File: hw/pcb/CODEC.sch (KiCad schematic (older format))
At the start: 55 parts, among them J501 AUEXT, J502 RIN, J503 LIN, J504 ROUT, J505 LOUT, U501 WM8731, U502 TL072, U503 TL072, Y501 11.289600

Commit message: wm8978 PCB design files
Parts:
- removed C521: 10u, Capacitor_SMD:C_0402_1005Metric, symbol Device:C
- removed J501: AUEXT, Connector_PinHeader_2.54mm:PinHeader_2x05_P2.54mm_Vertical_SMD, symbol Connector_Generic:Conn_02x05_Odd_Even
- removed U501: WM8731, Package_SO:SSOP-28_5.3x10.2mm_P0.65mm, symbol cirrus:WM8731
- removed Y501: 11.289600, Crystal:Crystal_SMD_3225-4Pin_3.2x2.5mm, symbol Device:Crystal_GND24
- added JP505: ROUT, Jumper:SolderJumper-3_P1.3mm_Open_RoundedPad1.0x1.5mm_NumberLabels, symbol Jumper:Jumper_3_Open
- added JP506: LOUT, Jumper:SolderJumper-3_P1.3mm_Open_RoundedPad1.0x1.5mm_NumberLabels, symbol Jumper:Jumper_3_Open
- added JP507: LIN, Jumper:SolderJumper-3_P1.3mm_Open_RoundedPad1.0x1.5mm_NumberLabels, symbol Jumper:Jumper_3_Open
- added JP508: RIN, Jumper:SolderJumper-3_P1.3mm_Open_RoundedPad1.0x1.5mm_NumberLabels, symbol Jumper:Jumper_3_Open
- added L501: 10uH, Capacitor_SMD:C_0603_1608Metric, symbol Device:L
- added U501: WM8978CGEFL_V, Package_DFN_QFN:QFN-32-1EP_5x5mm_P0.5mm_EP3.65x3.65mm_ThermalVias, symbol SamacSys_Parts:WM8978CGEFL_V
- C502, C514, C520: value 10u -> 100n
- C503, C508: value 100n -> 4.7u
- C505, C506: value 18p -> 4.7u
- C507: value 10u -> 4.7u
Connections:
- net labels added: +3.3VP, L2, MCLK, R2
- net labels removed: LHPOUT, MICBIAS, MICIN, RHPOUT
- wire segments 236 -> 221
- no-connect marks 5 -> 9
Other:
- note added: "Bridge solder jumpers on pin 2+3 for normal operations.\n1+2 is for testing and playing with the codec."
- note added: "Solder jumpers for DC coupling (not tested)"
- note added: "The output op amp section is based on\nMutable Instruments Clouds (c) Émilie Gillet"
- note added: "WM8978 ADC is MUCH BETTER than the WM8731:\nRead this also: https://hackaday.io/project/7936-cortex-guitar-board/log/44553-this-adc-makes-weird-noises\nIt strikes me that it is still used so often in Eurorack audio (I made that mistake too)"
- note removed: "This section is based on\nMutable Instruments Clouds (c) Émilie Gillet"
- note removed: "To external audio breakout.\nUseful for testing."
- moved on the sheet: C507, C511, C515, C516, C517, C522, C523, C524, J504, J505, JP503, JP504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

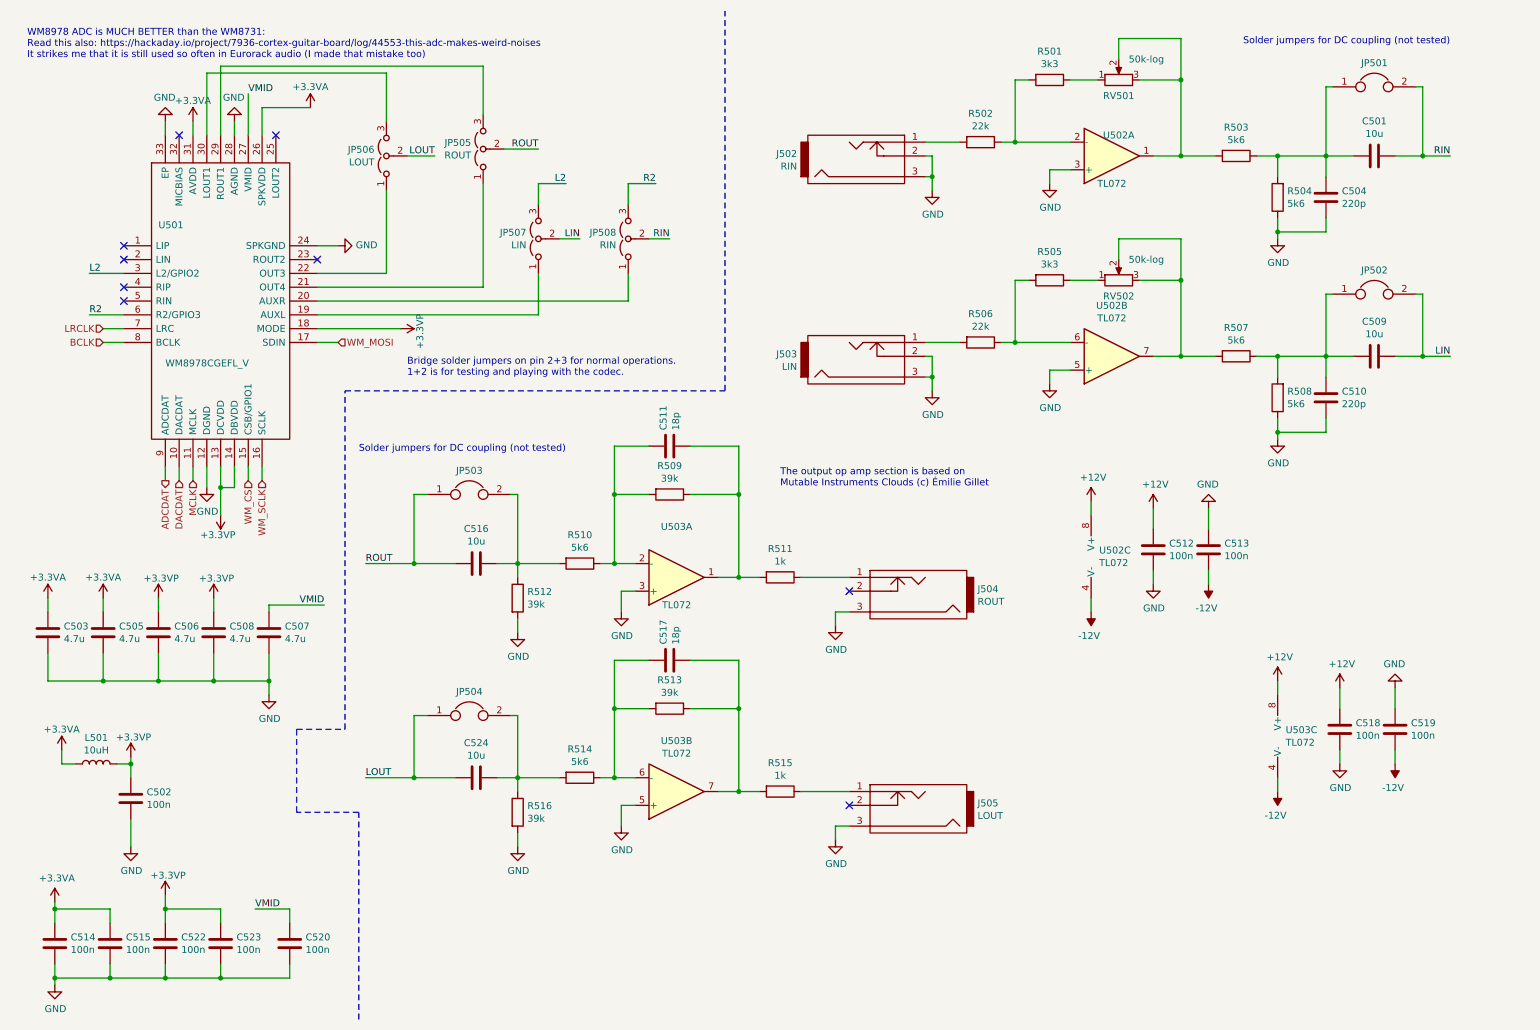
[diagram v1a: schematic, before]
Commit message: fixed severe PCB issue, clearance of ground fills was too small, could lead to thermal instability
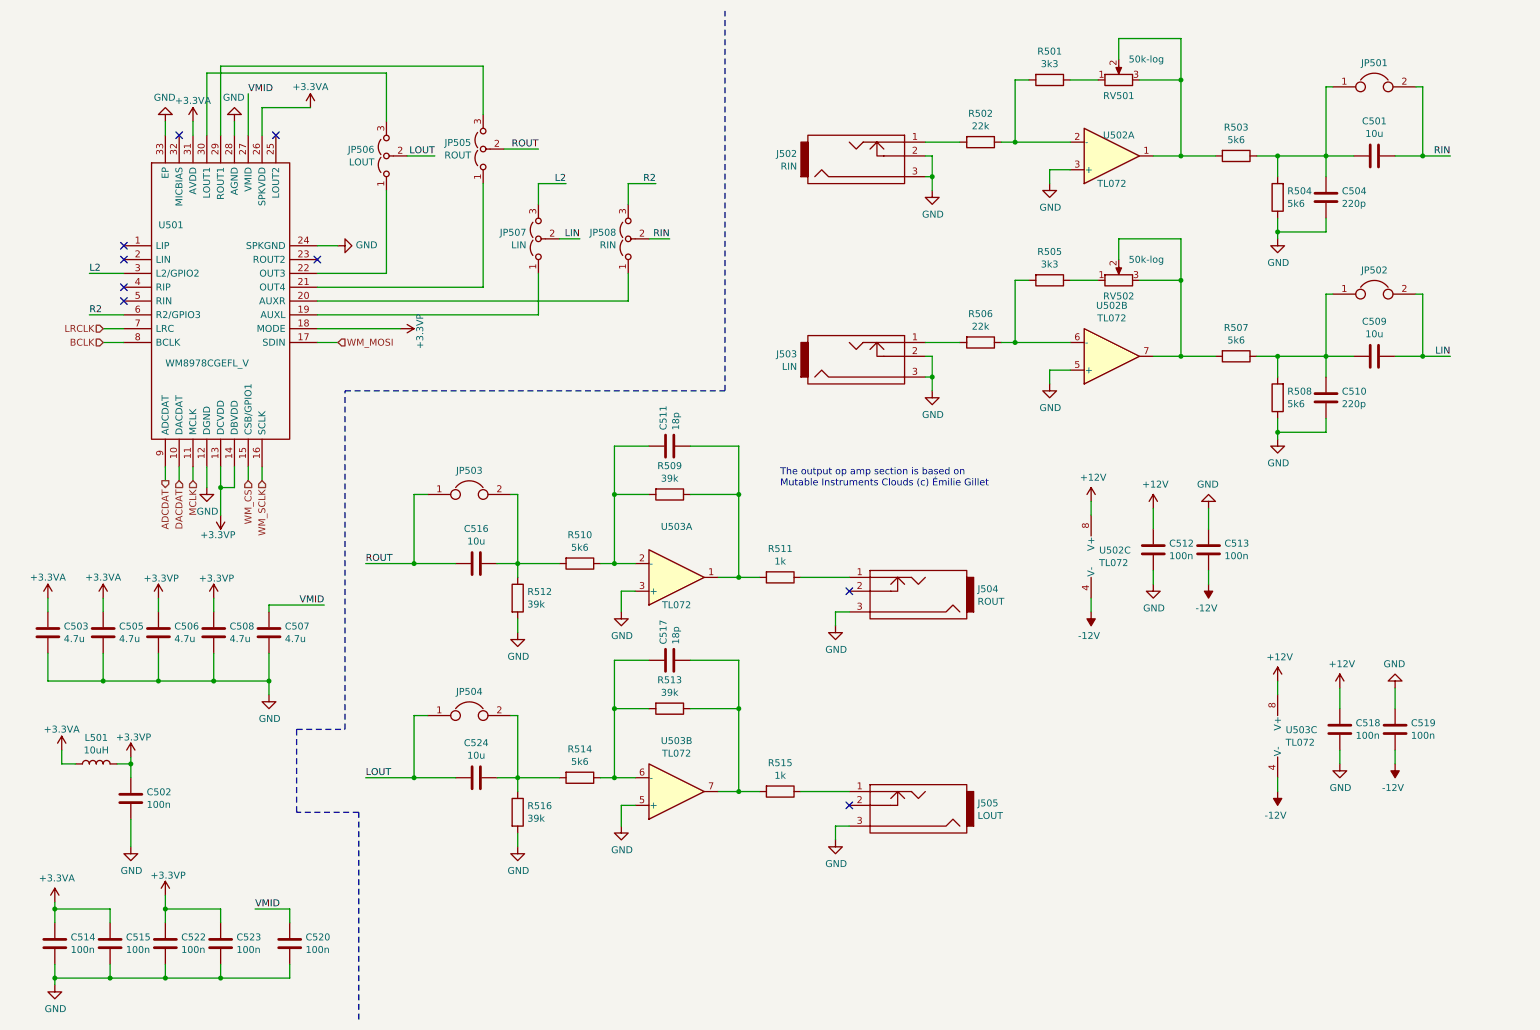
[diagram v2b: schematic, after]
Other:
- note removed: "Bridge solder jumpers on pin 2+3 for normal operations.\n1+2 is for testing and playing with the codec."
- note removed: "Solder jumpers for DC coupling (not tested)"
- note removed: "WM8978 ADC is MUCH BETTER than the WM8731:\nRead this also: https://hackaday.io/project/7936-cortex-guitar-board/log/44553-this-adc-makes-weird-noises\nIt strikes me that it is still used so often in Eurorack audio (I made that mistake too)"
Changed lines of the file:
@@
 encoding utf-8
 Sheet 5 6
-Title "CTAG-TBD"
-Date "2020-06-06"
-Rev "C"
+Title "ESP32 Eurorack Audio Module"
+Date "2020-08-18"
+Rev "G"
 Comp "(c) Robert Manzke 2020"
 Comment1 "https://creativecommons.org/licenses/by-nc-sa/4.0/"
@@
 Wire Wire Line
 	4300 2650 4300 2350
-Text Notes 600  800  0    50   ~ 0
-WM8978 ADC is MUCH BETTER than the WM8731:\nRead this also: https://hackaday.io/project/7936-cortex-guitar-board/log/44553-this-adc-makes-weird-noises\nIt strikes me that it is still used so often in Eurorack audio (I made that mistake too)
-Text Notes 3000 3650 0    50   ~ 0
-Solder jumpers for DC coupling (not tested)
-Text Notes 9400 700  0    50   ~ 0
-Solder jumpers for DC coupling (not tested)
-Text Notes 3350 3100 0    50   ~ 0
-Bridge solder jumpers on pin 2+3 for normal operations.\n1+2 is for testing and playing with the codec.
 $EndSCHEMATC

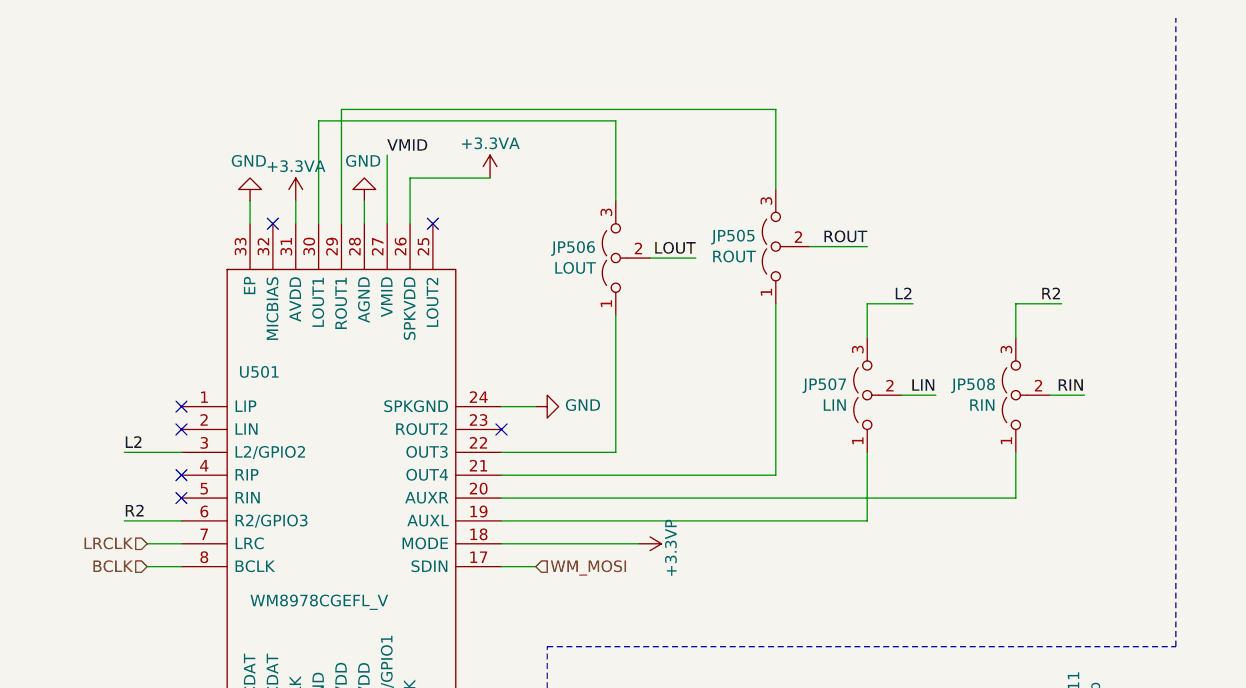
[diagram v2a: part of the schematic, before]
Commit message: Updated Eurorack hw to Rev. H
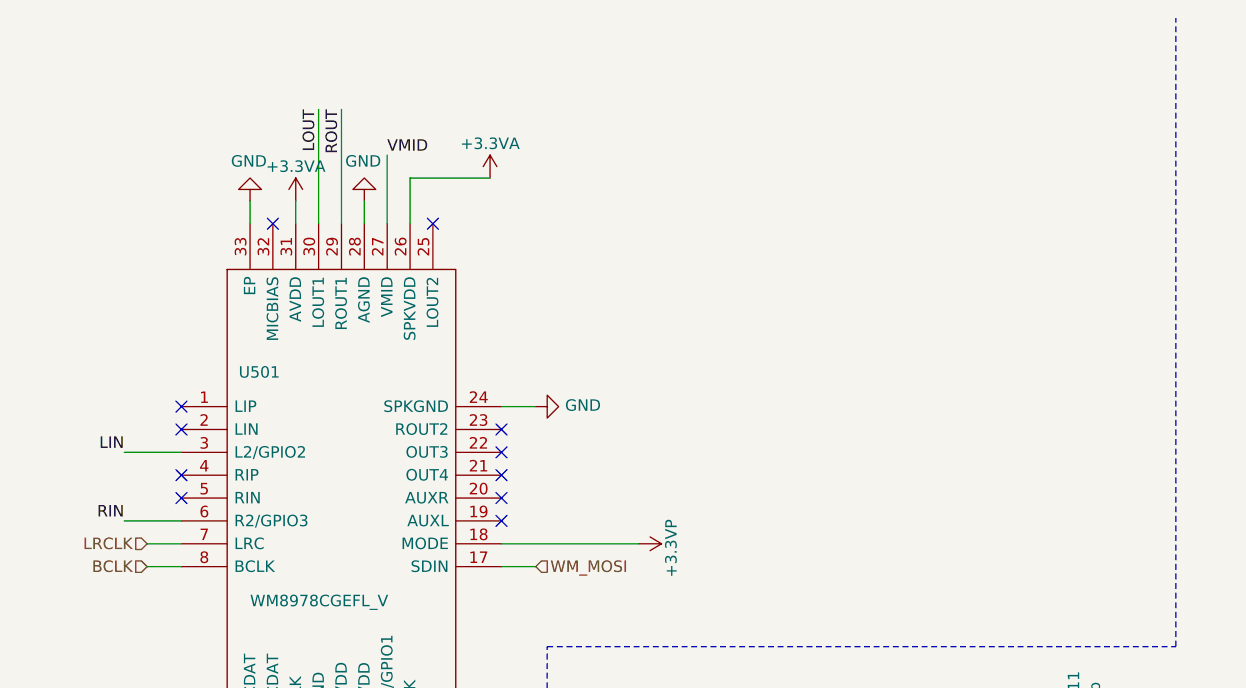
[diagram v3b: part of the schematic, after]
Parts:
- removed JP505: ROUT, Jumper:SolderJumper-3_P1.3mm_Open_RoundedPad1.0x1.5mm_NumberLabels, symbol Jumper:Jumper_3_Open
- removed JP506: LOUT, Jumper:SolderJumper-3_P1.3mm_Open_RoundedPad1.0x1.5mm_NumberLabels, symbol Jumper:Jumper_3_Open
- removed JP507: LIN, Jumper:SolderJumper-3_P1.3mm_Open_RoundedPad1.0x1.5mm_NumberLabels, symbol Jumper:Jumper_3_Open
- removed JP508: RIN, Jumper:SolderJumper-3_P1.3mm_Open_RoundedPad1.0x1.5mm_NumberLabels, symbol Jumper:Jumper_3_Open
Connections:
- net L2 is gone; now on net LIN: U501.3 (L2/GPIO2)
- net R2 is gone; now on net RIN: U501.6 (R2/GPIO3)
- net LOUT: now also U501.30 (LOUT1)
- net ROUT: now also U501.29 (ROUT1)
- no-connect marks 9 -> 13
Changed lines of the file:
@@
 Sheet 5 6
 Title "ESP32 Eurorack Audio Module"
-Date "2020-08-18"
-Rev "G"
-Comp "(c) Robert Manzke 2020"
+Date "2021-10-05"
+Rev "H"
+Comp "(c) Robert Manzke 2021"
 Comment1 "https://creativecommons.org/licenses/by-nc-sa/4.0/"
 Comment2 "Licensed under CC BY-NC-SA 4.0"
@@
 Wire Wire Line
 	2350 4750 2750 4750
-Wire Wire Line
-	4050 1450 4300 1450
-Text Label 3550 1500 2    50   ~ 0
+Text Label 1900 850  3    50   ~ 0
 LOUT
-Text Label 4300 1450 2    50   ~ 0
+Text Label 2000 850  3    50   ~ 0
 ROUT
 Text Label 2750 4750 2    50   ~ 0
@@
 Wire Wire Line
 	5750 3950 5750 4550
-Wire Wire Line
-	3700 4450 3400 4450
 Text Label 3050 4450 0    50   ~ 0
 ROUT
@@
 	7150 2950 7150 3100
 Connection ~ 7150 3100
-Wire Wire Line
-	3350 1500 3550 1500
 $Comp
 L power:GND #PWR0507
@@
 Wire Wire Line
 	10700 2950 10900 2950
-$Comp
-L Device:Jumper JP503
-U 1 1 5DD9E741
-P 3800 3950
-F 0 "JP503" H 3800 4123 50  0000 C CNN
-F 1 "~" H 3800 4123 50  0000 C CNN
-F 2 "Jumper:SolderJumper-2_P1.3mm_Open_RoundedPad1.0x1.5mm" H 3800 3950 50  0001 C CNN
-F 3 "~" H 3800 3950 50  0001 C CNN
-	1    3800 3950
-	1    0    0    -1
-$EndComp
 Wire Wire Line
 	4100 3950 4150 3950
-Wire Wire Line
-	4150 3950 4150 4450
-Wire Wire Line
-	3500 3950 3400 3950
-Wire Wire Line
-	3400 3950 3400 4450
-Connection ~ 3400 4450
-Wire Wire Line
-	3400 4450 3050 4450
 $Comp
 L Device:Jumper JP504
@@
 	2850 2150 2700 2150
 NoConn ~ 2700 2250
-$Comp
-L Jumper:Jumper_3_Open JP506
-U 1 1 5E77595A
-P 3200 1500
-F 0 "JP506" V 3246 1587 50  0000 L CNN
-F 1 "LOUT" V 3155 1587 50  0000 L CNN
-F 2 "Jumper:SolderJumper-3_P1.3mm_Open_RoundedPad1.0x1.5mm_NumberLabels" H 3200 1500 50  0001 C CNN
-F 3 "~" H 3200 1500 50  0001 C CNN
-	1    3200 1500
-	0    -1   -1   0
-$EndComp
-$Comp
-L Jumper:Jumper_3_Open JP505
-U 1 1 5E78AD6A
-P 3900 1450
-F 0 "JP505" V 3946 1537 50  0000 L CNN
-F 1 "ROUT" V 3855 1537 50  0000 L CNN
-F 2 "Jumper:SolderJumper-3_P1.3mm_Open_RoundedPad1.0x1.5mm_NumberLabels" H 3900 1450 50  0001 C CNN
-F 3 "~" H 3900 1450 50  0001 C CNN
-	1    3900 1450
-	0    -1   -1   0
-$EndComp
-Wire Wire Line
-	2700 2350 3200 2350
-Wire Wire Line
-	3200 2350 3200 1750
-Wire Wire Line
-	2700 2450 3900 2450
-Wire Wire Line
-	3900 2450 3900 1700
-Wire Wire Line
-	3200 1250 3200 900
-Wire Wire Line
-	3200 900  1900 900
-Wire Wire Line
-	1900 900  1900 1350
-Wire Wire Line
-	3900 1200 3900 850
-Wire Wire Line
-	3900 850  2000 850
+Wire Wire Line
+	1900 850  1900 1350
 Wire Wire Line
 	2000 850  2000 1350
@@
 Wire Wire Line
 	1300 2650 1050 2650
-Text Label 1050 2350 0    50   ~ 0
-L2
-Text Label 1050 2650 0    50   ~ 0
-R2
-Wire Wire Line
-	4300 1700 4500 1700
-Wire Wire Line
-	4950 1700 5150 1700
-Text Label 4500 1700 2    50   ~ 0
-L2
-Text Label 5150 1700 2    50   ~ 0
-R2
 NoConn ~ 1700 1350
 NoConn ~ 2400 1350
@@
 Wire Wire Line
 	2300 1150 2300 1350
-Wire Wire Line
-	4950 1850 4950 1700
-Wire Wire Line
-	4300 1850 4300 1700
-$Comp
-L Jumper:Jumper_3_Open JP508
-U 1 1 5E807B21
-P 4950 2100
-F 0 "JP508" V 4996 2187 50  0000 L CNN
-F 1 "RIN" V 4905 2187 50  0000 L CNN
-F 2 "Jumper:SolderJumper-3_P1.3mm_Open_RoundedPad1.0x1.5mm_NumberLabels" H 4950 2100 50  0001 C CNN
-F 3 "~" H 4950 2100 50  0001 C CNN
-	1    4950 2100
-	0    -1   -1   0
-$EndComp
-$Comp
-L Jumper:Jumper_3_Open JP507
-U 1 1 5E7FBA3C
-P 4300 2100
-F 0 "JP507" V 4346 2187 50  0000 L CNN
-F 1 "LIN" V 4255 2187 50  0000 L CNN
-F 2 "Jumper:SolderJumper-3_P1.3mm_Open_RoundedPad1.0x1.5mm_NumberLabels" H 4300 2100 50  0001 C CNN
-F 3 "~" H 4300 2100 50  0001 C CNN
-	1    4300 2100
-	0    -1   -1   0
-$EndComp
-Text Label 5250 2100 2    50   ~ 0
+Text Label 1050 2650 2    50   ~ 0
 RIN
-Text Label 4600 2100 2    50   ~ 0
+Text Label 1050 2350 2    50   ~ 0
 LIN
-Wire Wire Line
-	5100 2100 5250 2100
-Wire Wire Line
-	4450 2100 4600 2100
-Wire Wire Line
-	4950 2550 4950 2350
-Wire Wire Line
-	2700 2550 4950 2550
-Wire Wire Line
-	2700 2650 4300 2650
-Wire Wire Line
-	4300 2650 4300 2350
+NoConn ~ 2700 2350
+NoConn ~ 2700 2450
+NoConn ~ 2700 2550
+NoConn ~ 2700 2650
+Wire Wire Line
+	4150 3950 4150 4450
+Wire Wire Line
+	3400 4450 3050 4450
+Wire Wire Line
+	3700 4450 3400 4450
+Connection ~ 3400 4450
+Wire Wire Line
+	3400 3950 3400 4450
+Wire Wire Line
+	3500 3950 3400 3950
+$Comp
+L Device:Jumper JP503
+U 1 1 5DD9E741
+P 3800 3950
+F 0 "JP503" H 3800 4123 50  0000 C CNN
+F 1 "~" H 3800 4123 50  0000 C CNN
+F 2 "Jumper:SolderJumper-2_P1.3mm_Open_RoundedPad1.0x1.5mm" H 3800 3950 50  0001 C CNN
+F 3 "~" H 3800 3950 50  0001 C CNN
+	1    3800 3950
+	1    0    0    -1
+$EndComp
 $EndSCHEMATC
